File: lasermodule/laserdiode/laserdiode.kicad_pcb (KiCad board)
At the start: 2 copper layers, 33.3 x 17.5 mm, 15 parts, among them J1 Conn_01x04, J2 Conn_01x01, J3 Conn_01x01, J4 Conn_01x01, J5 Conn_01x01, J6 Conn_01x01, J7 Conn_01x01

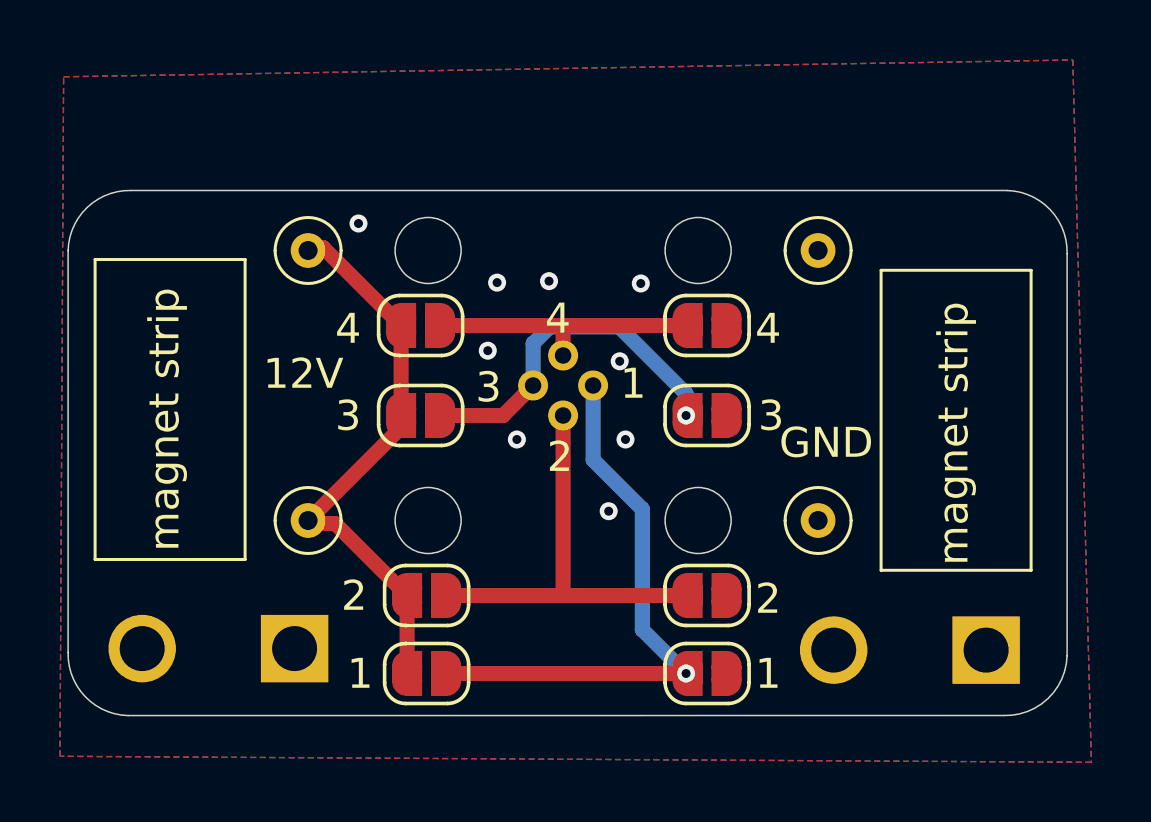
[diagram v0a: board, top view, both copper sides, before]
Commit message: fixed typo, added standoff lasermodule
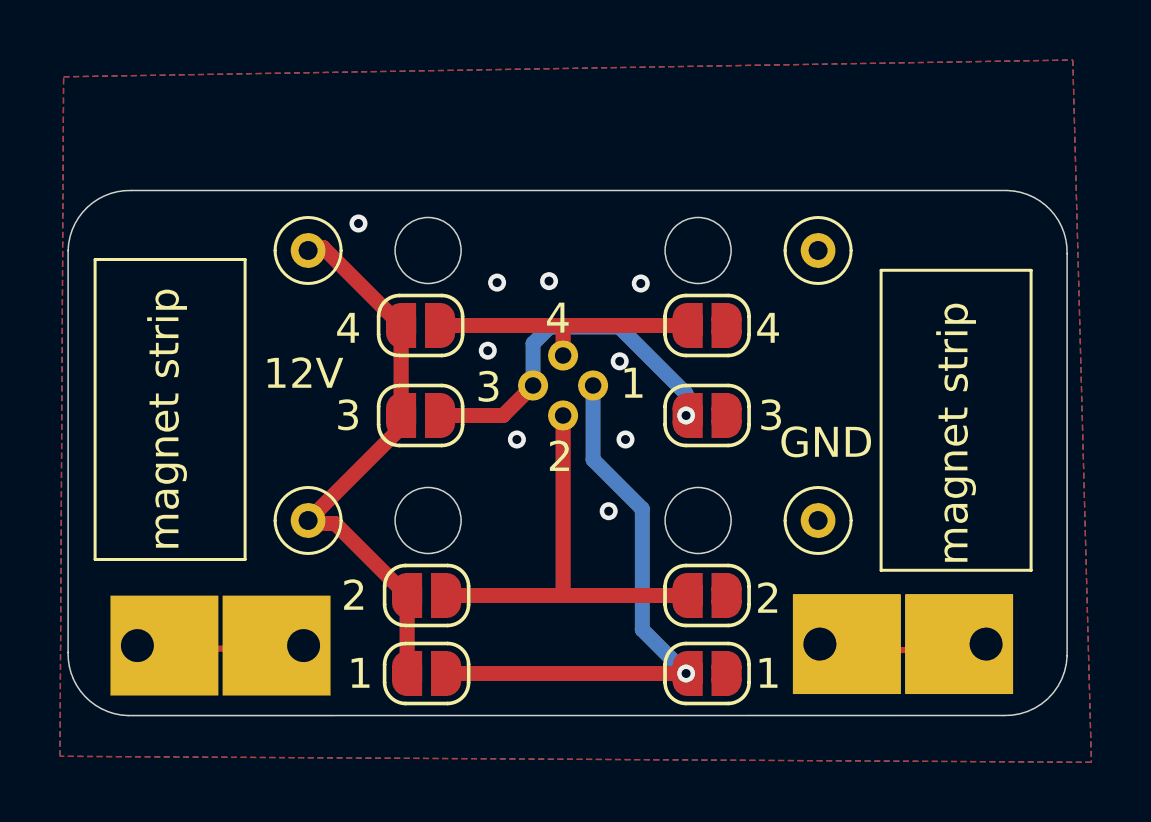
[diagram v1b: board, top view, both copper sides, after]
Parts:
- moved J6 0.32 mm to (136.3, 97.7)
- moved J7 0.20 mm to (159.1, 97.6)
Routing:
- net unconnected-(J6-Pin_1-Pad1): track 0.59 -> 6.13 mm
- net unconnected-(J7-Pin_1-Pad1): track 0.00 -> 5.54 mm

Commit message: changes to reduce prices pcbway
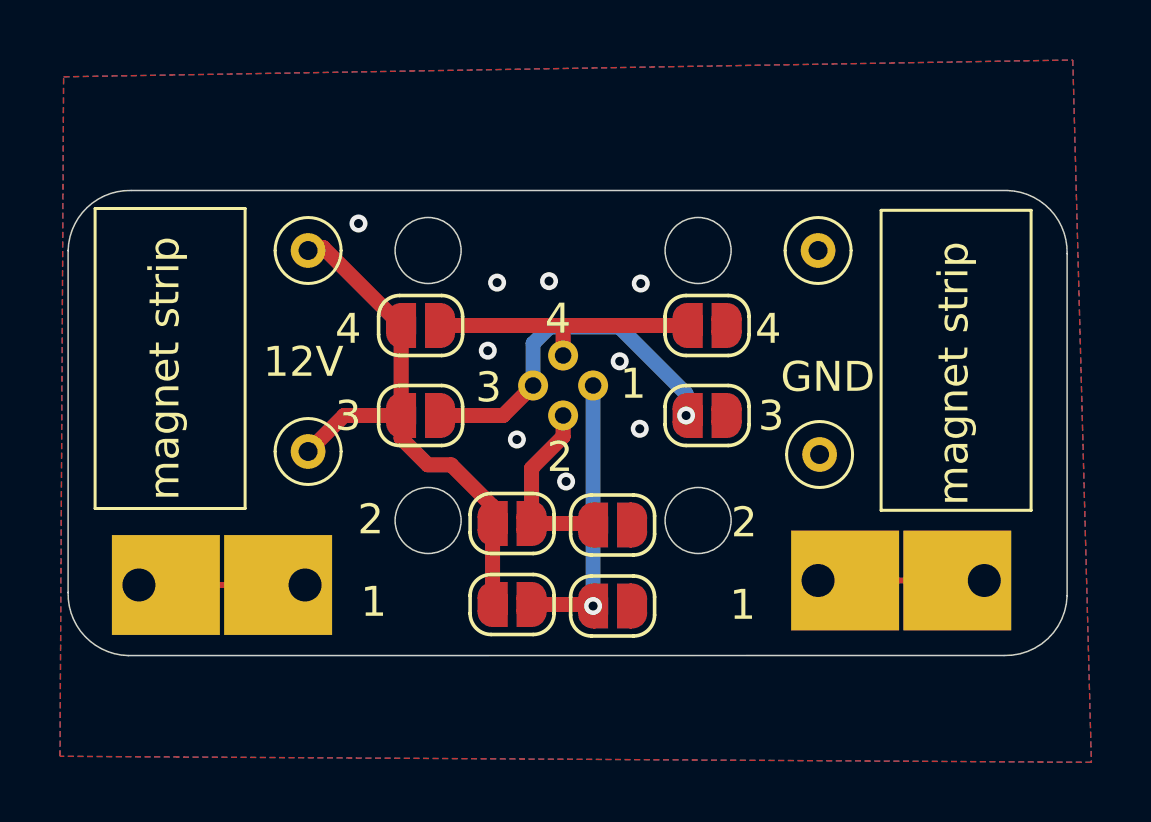
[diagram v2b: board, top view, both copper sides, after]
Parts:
- moved JP6 3.93 mm to (146.7, 93.7)
- moved JP8 3.87 mm to (146.7, 96.3)
- moved JP5 3.73 mm to (143.3, 93.6)
- moved JP7 3.66 mm to (143.3, 96.3)
- moved J5 2.30 mm to (136.5, 91.2)
- moved J3 2.20 mm to (153.6, 91.3)
- moved J7 2.12 mm to (159.0, 95.5)
- moved J6 2.02 mm to (136.4, 95.7)
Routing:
- net Net-(J1-Pin_1): track 18.9 -> 9.42 mm
- net Net-(J1-Pin_2): track 14.1 -> 6.11 mm
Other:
- board size 33.3 x 17.5 mm -> 33.3 x 15.5 mm
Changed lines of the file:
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@@
 	(footprint "Jumper:SolderJumper-2_P1.3mm_Open_RoundedPad1.0x1.5mm"
 		(layer "F.Cu")
-		(at 149.8 98.6)
+		(at 146.65 96.35)
 		(descr "SMD Solder Jumper, 1x1.5mm, rounded Pads, 0.3mm gap, open")
 		(tags "solder jumper open")
@@
 	(footprint "laserdiode:0906115207514110"
 		(layer "F.Cu")
-		(at 153.5 93.5)
+		(at 153.55 91.3)
 		(descr "0906-1-15-20-75-14-11-0-1")
 		(tags "Connector")
@@
 	(footprint "Jumper:SolderJumper-2_P1.3mm_Open_RoundedPad1.0x1.5mm"
 		(layer "F.Cu")
-		(at 140.45 98.6 180)
+		(at 143.3 96.3 180)
 		(descr "SMD Solder Jumper, 1x1.5mm, rounded Pads, 0.3mm gap, open")
 		(tags "solder jumper open")
@@
 	(footprint "Jumper:SolderJumper-2_P1.3mm_Open_RoundedPad1.0x1.5mm"
 		(layer "F.Cu")
-		(at 149.8 96)
+		(at 146.65 93.65)
 		(descr "SMD Solder Jumper, 1x1.5mm, rounded Pads, 0.3mm gap, open")
 		(tags "solder jumper open")
@@
 	(footprint "laserdiode:0906115207514110"
 		(layer "F.Cu")
-		(at 136.5 93.5)
+		(at 136.5 91.2)
 		(descr "0906-1-15-20-75-14-11-0-1")
 		(tags "Connector")
@@
 	(footprint "Jumper:SolderJumper-2_P1.3mm_Open_RoundedPad1.0x1.5mm"
 		(layer "F.Cu")
-		(at 140.45 96 180)
+		(at 143.3 93.6 180)
 		(descr "SMD Solder Jumper, 1x1.5mm, rounded Pads, 0.3mm gap, open")
 		(tags "solder jumper open")
@@
 	(footprint "laserdiode:23765912"
 		(layer "B.Cu")
-		(at 136.35 97.67 180)
+		(at 136.4 95.65 180)
 		(descr "2376591-2-1")
 		(tags "Connector")
@@
 	(footprint "laserdiode:23765912"
 		(layer "B.Cu")
-		(at 159.1 97.62 180)
+		(at 159.04 95.5 180)
 		(descr "2376591-2-1")
 		(tags "Connector")
@@
 	)
 	(gr_rect
-		(start 129.4 84.8)
-		(end 134.4 94.8)
+		(start 129.4 83.1)
+		(end 134.4 93.1)
 		(stroke
 			(width 0.1)
@@
 	)
 	(gr_rect
-		(start 155.6 85.16)
-		(end 160.6 95.16)
+		(start 155.6 83.16)
+		(end 160.6 93.16)
 		(stroke
 			(width 0.1)
@@
 	(gr_line
 		(start 161.8 84.602498)
-		(end 161.8 98.01)
+		(end 161.8 96.01)
 		(stroke
 			(width 0.05)
@@
 	(gr_line
 		(start 128.5 84.5)
-		(end 128.5 97.9)
+		(end 128.5 95.9)
 		(stroke
 			(width 0.05)
@@
 	)
 	(gr_arc
-		(start 161.8 98.01)
-		(mid 161.159541 99.439094)
-		(end 159.697495 100.000274)
+		(start 161.8 96.01)
+		(mid 161.159541 97.439094)
+		(end 159.697495 98.000274)
 		(stroke
 			(width 0.05)
@@
 	)
 	(gr_line
-		(start 130.5 100.002498)
-		(end 159.697495 100.000274)
+		(start 130.5 98.002498)
+		(end 159.697495 98.000274)
 		(stroke
 			(width 0.05)
@@
 	)
 	(gr_arc
-		(start 130.5 100.002498)
-		(mid 129.064545 99.365476)
-		(end 128.5 97.9)
+		(start 130.5 98.002498)
+		(mid 129.064546 97.365476)
+		(end 128.5 95.9)
 		(stroke
 			(width 0.05)
@@
 	)
 	(gr_text "1"
-		(at 137.8 99.2 0)
+		(at 138.25 96.8 0)
 		(layer "F.SilkS")
 		(effects
@@
 	)
 	(gr_text "2"
-		(at 151.4 96.7 0)
+		(at 150.6 94.15 0)
 		(layer "F.SilkS")
 		(effects
@@
 	)
 	(gr_text "1"
-		(at 151.4 99.2 0)
+		(at 150.55 96.9 0)
 		(layer "F.SilkS")
 		(effects
@@
 	)
 	(gr_text "GND"
-		(at 152.2 91.5 0)
+		(at 152.25 89.3 0)
 		(layer "F.SilkS")
 		(effects
@@
 	)
 	(gr_text "12V"
-		(at 135 89.2 0)
+		(at 135 88.8 0)
 		(layer "F.SilkS")
 		(effects
@@
 	)
 	(gr_text "magnet strip"
-		(at 132.3 94.531172 90)
+		(at 132.3 92.831172 90)
 		(layer "F.SilkS")
 		(effects
@@
 	)
 	(gr_text "2"
-		(at 137.6 96.6 0)
+		(at 138.15 94.05 0)
 		(layer "F.SilkS")
 		(effects
@@
 	)
 	(gr_text "magnet strip"
-		(at 158.6 95 90)
+		(at 158.6 93 90)
 		(layer "F.SilkS")
 		(effects
@@
 	)
 	(segment
-		(start 141.1 96)
-		(end 145.1 96)
+		(start 143.95 91.757106)
+		(end 143.95 93.6)
 		(width 0.5)
 		(layer "F.Cu")
@@
 	)
 	(segment
-		(start 145 95.9)
-		(end 145.1 96)
+		(start 145 90.707106)
+		(end 143.95 91.757106)
 		(width 0.5)
 		(layer "F.Cu")
@@
 	)
 	(segment
-		(start 145.1 96)
-		(end 149.15 96)
+		(start 145.95 93.6)
+		(end 146 93.65)
 		(width 0.5)
 		(layer "F.Cu")
@@
 	(segment
 		(start 145 90)
-		(end 145 95.9)
+		(end 145 90.707106)
 		(width 0.5)
 		(layer "F.Cu")
@@
 	)
 	(segment
-		(start 141.1 98.6)
-		(end 149.15 98.6)
+		(start 143.95 93.6)
+		(end 145.95 93.6)
 		(width 0.5)
 		(layer "F.Cu")
-		(net 4)
-	)
-	(via
-		(at 149.1 98.6)
-		(size 0.6)
-		(drill 0.3)
-		(layers "F.Cu" "B.Cu")
-		(net 4)
+		(net 3)
 	)
 	(segment
-		(start 147.639064 97.139064)
-		(end 149.1 98.6)
+		(start 145.95 96.3)
+		(end 143.95 96.3)
 		(width 0.5)
-		(layer "B.Cu")
+		(layer "F.Cu")
 		(net 4)
 	)
 	(segment
-		(start 146 89)
-		(end 146 91.475122)
+		(start 146 96.35)
+		(end 145.95 96.3)
 		(width 0.5)
-		(layer "B.Cu")
+		(layer "F.Cu")
+		(net 4)
+	)
+	(via
+		(at 145.999988 96.349994)
+		(size 0.6)
+		(drill 0.3)
+		(layers "F.Cu" "B.Cu")
 		(net 4)
 	)
 	(segment
-		(start 146 91.475122)
-		(end 147.639064 93.114186)
+		(start 146 96.349982)
+		(end 145.999988 96.349994)
 		(width 0.5)
 		(layer "B.Cu")
@@
 	)
 	(segment
-		(start 147.639064 93.114186)
-		(end 147.639064 97.139064)
+		(start 146 89)
+		(end 146 96.349982)
 		(width 0.5)
 		(layer "B.Cu")
@@
 	)
 	(via
-		(at 147.08 90.8)
+		(at 147.555527 90.442784)
 		(size 0.6)
 		(drill 0.3)
@@
 	)
 	(via
-		(at 146.52 93.19)
+		(at 145.1 92.2)
 		(size 0.6)
 		(drill 0.3)
@@
 	)
 	(segment
-		(start 139.6 90.4)
-		(end 136.4 93.6)
+		(start 141.269964 91.644909)
+		(end 142.65 93.024945)
 		(width 0.5)
 		(layer "F.Cu")
@@
 	)
 	(segment
-		(start 139.8 98.6)
-		(end 139.8 96)
+		(start 140.489909 91.644909)
+		(end 141.269964 91.644909)
 		(width 0.5)
 		(layer "F.Cu")
@@
 	)
 	(segment
-		(start 137.4 93.6)
-		(end 139.8 96)
+		(start 139.6 90.755)
+		(end 140.489909 91.644909)
 		(width 0.5)
 		(layer "F.Cu")
@@
 	)
 	(segment
-		(start 137 84.4)
-		(end 139.6 87)
+		(start 139.6 90)
+		(end 137.7 90)
 		(width 0.5)
 		(layer "F.Cu")
@@
 	)
 	(segment
-		(start 136.4 93.6)
-		(end 137.4 93.6)
+		(start 139.6 90)
+		(end 139.6 90.755)
 		(width 0.5)
 		(layer "F.Cu")
@@
 	)
 	(segment
-		(start 139.6 90)
-		(end 139.6 90.4)
+		(start 142.65 93.6)
+		(end 142.65 96.3)
+		(width 0.5)
+		(layer "F.Cu")
+		(net 6)
+	)
+	(segment
+		(start 142.65 93.024945)
+		(end 142.65 93.6)
+		(width 0.5)
+		(layer "F.Cu")
+		(net 6)
+	)
+	(segment
+		(start 137 84.4)
+		(end 139.6 87)
+		(width 0.5)
+		(layer "F.Cu")
+		(net 6)
+	)
+	(segment
+		(start 137.7 90)
+		(end 136.5 91.2)
 		(width 0.5)
 		(layer "F.Cu")
@@
 	)
 	(segment
-		(start 130.51 97.77)
-		(end 136.05 97.77)
+		(start 130.51 96)
+		(end 130.86 95.65)
 		(width 0.2)
 		(layer "F.Cu")
@@
 	)
 	(segment
-		(start 136.1 97.73)
-		(end 136.52 98.15)
-		(width 0.5)
+		(start 130.86 95.65)
+		(end 136.05 95.65)
+		(width 0.2)
 		(layer "F.Cu")
 		(net 7)
 	)
 	(segment
-		(start 153.56 97.82)
-		(end 159.1 97.82)
+		(start 153.5 95.5)
+		(end 159.04 95.5)
 		(width 0.2)
 		(layer "F.Cu")
